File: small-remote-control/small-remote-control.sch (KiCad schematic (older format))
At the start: 9 parts, among them J1 AudioJack4, SW1 A, SW2 B, SW3 C, SW4 D

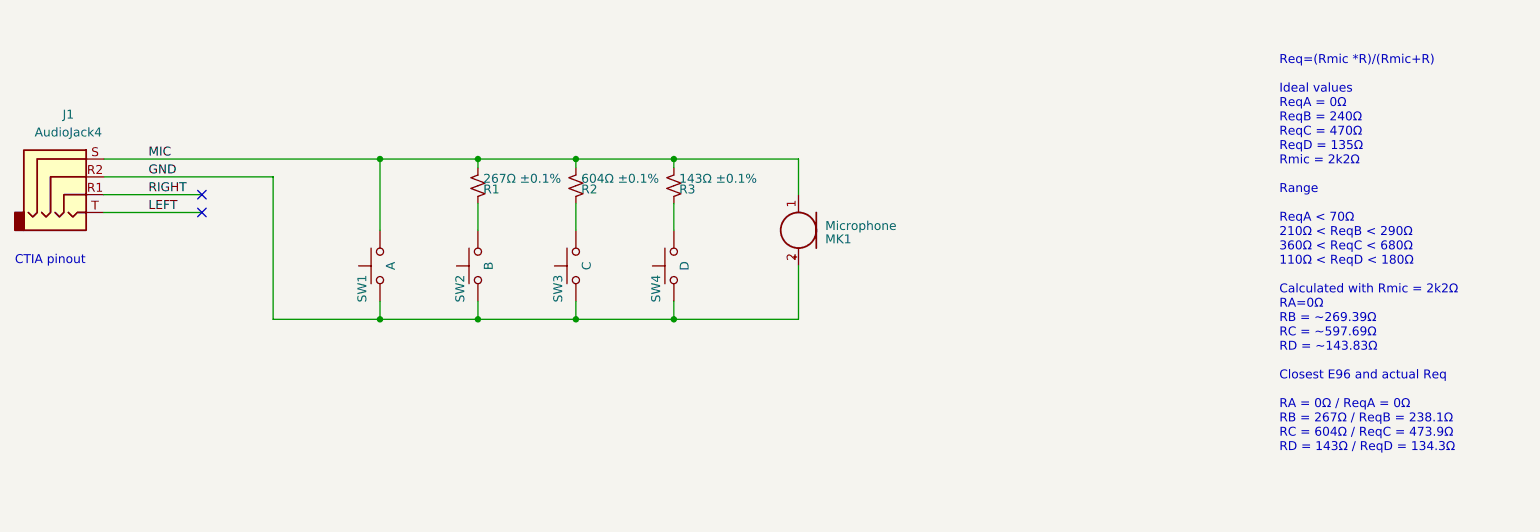
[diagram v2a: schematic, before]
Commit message: removed mic and switch D, added 2.2kΩ resistor
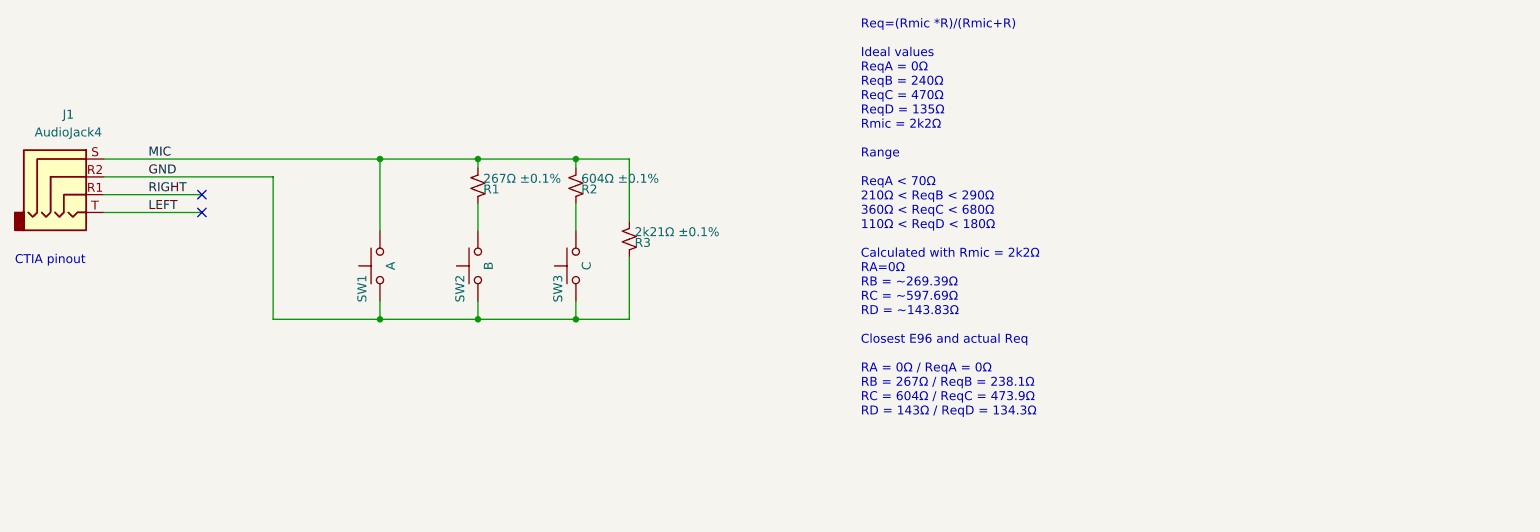
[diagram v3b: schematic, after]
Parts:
- removed MK1: Microphone, SW-CUI-INC:CMC-4015-40P, symbol Device:Microphone
- removed SW4: D, SW-Omron:B3W-6x6mm-NG, symbol Switch:SW_Push
- R3: value 143Ω ±0.1% -> 2k21Ω ±0.1%; Description RES 143 OHM 0.1% 1/10W 0402 -> RES 2.21K OHM 0.1% 1/10W 0402; MPN RP73PF1E143RBTD -> RP73PF1E2K21BTD
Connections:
- net GND: now also R3.1
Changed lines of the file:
@@
-$EndComp
-$Comp
-L Switch:SW_Push SW4
-U 1 1 5F24FFE6
-P 4600 3350
-F 0 "SW4" H 4650 3450 50  0000 L CNN
-F 1 "D" H 4600 3290 50  0000 C CNN
-F 2 "SW-Omron:B3W-6x6mm-NG" H 4600 3550 50  0001 C CNN
-F 3 "https://omronfs.omron.com/en_US/ecb/products/pdf/en-b3w.pdf" H 4600 3550 50  0001 C CNN
-F 4 "B3W-1002" H 4600 3350 50  0001 C CNN "MPN"
-F 5 "SWITCH TACTILE SPST-NO 0.05A 24V" H 4600 3350 50  0001 C CNN "Description"
-F 6 "Omron Electronics Inc-EMC Div" H 4600 3350 50  0001 C CNN "Manufacturer"
-F 7 "Digikey" H 4600 3350 50  0001 C CNN "Source"
-	1    4600 3350
-	0    -1   1    0
-$EndComp
-$Comp
-L Device:Microphone MK1
-U 1 1 5F25357C
-P 5300 3150
-F 0 "MK1" H 5150 3200 50  0000 R CNN
-F 1 "Microphone" H 5150 3125 50  0000 R CNN
-F 2 "SW-CUI-INC:CMC-4015-40P" V 5300 3250 50  0001 C CNN
-F 3 "https://www.cuidevices.com/product/resource/cmc-4015-40p.pdf" V 5300 3250 50  0001 C CNN
-F 4 "CUI Devices" H 5300 3150 50  0001 C CNN "Manufacturer"
-F 5 "Digikey" H 5300 3150 50  0001 C CNN "Source"
-F 6 "CMC-4015-40P" H 5300 3150 50  0001 C CNN "MPN"
-F 7 "(-40dB ±3dB @ 94dB SPL)" H 5300 3150 50  0001 C CNN "Characteristics"
-F 8 "100Hz ~ 20kHz Analog Microphone Electret Condenser 2V ~ 10V Omnidirectional (-40dB ±3dB @ 94dB SPL) PC Pins" H 5300 3150 50  0001 C CNN "Description"
-	1    5300 3150
-	-1   0    0    1
 $EndComp
 $Comp
@@
 	1    0    0    1
 $EndComp
-$Comp
-L Device:R_Small_US R3
-U 1 1 5F254B04
-P 4600 2900
-F 0 "R3" H 4630 2920 50  0000 L CNN
-F 1 "143Ω ±0.1%" H 4630 2860 50  0000 L CNN
-F 2 "Resistor_SMD:R_0402_1005Metric" H 4600 2900 50  0001 C CNN
-F 3 "~" H 4600 2900 50  0001 C CNN
-F 4 "TE Connectivity" H 4600 2900 50  0001 C CNN "Manufacturer"
-F 5 "0402/1005M" H 4600 2900 50  0001 C CNN "Package ID"
-F 6 "Digikey" H 4600 2900 50  0001 C CNN "Source"
-F 7 "RP73PF1E143RBTD" H 4600 2900 50  0001 C CNN "MPN"
-F 8 "RES 143 OHM 0.1% 1/10W 0402" H 4600 2900 50  0001 C CNN "Description"
-F 9 "0.1% 1/10W" H 4600 2900 50  0001 C CNN "Characteristics"
-	1    4600 2900
-	1    0    0    1
-$EndComp
 Text Label 1650 3050 0    50   ~ 0
 LEFT
@@
 Text Notes 900  3350 0    50   ~ 0
 CTIA pinout
-Text Notes 8000 4400 0    50   ~ 0
+Text Notes 5650 4200 0    50   ~ 0
 Req=(Rmic *R)/(Rmic+R)\n\nIdeal values\nReqA = 0Ω\nReqB = 240Ω\nReqC = 470Ω\nReqD = 135Ω\nRmic = 2k2Ω\n\nRange\n\nReqA < 70Ω\n210Ω < ReqB < 290Ω\n360Ω < ReqC < 680Ω\n110Ω < ReqD < 180Ω\n\nCalculated with Rmic = 2k2Ω\nRA=0Ω\nRB = ~~269.39Ω\nRC = ~~597.69Ω\nRD = ~~143.83Ω\n\nClosest E96 and actual Req\n\nRA = 0Ω / ReqA = 0Ω\nRB = 267Ω / ReqB = 238.1Ω\nRC = 604Ω / ReqC = 473.9Ω\nRD = 143Ω / ReqD = 134.3Ω
-Wire Wire Line
-	4600 2750 4600 2800
 Wire Wire Line
 	1400 2750 2950 2750
@@
 	4050 2800 4050 2750
 Connection ~ 4050 2750
-Wire Wire Line
-	4050 2750 4600 2750
 Wire Wire Line
 	3500 2800 3500 2750
@@
 	2950 2750 3500 2750
 Wire Wire Line
-	5300 2950 5300 2750
-Wire Wire Line
-	5300 2750 4600 2750
-Connection ~ 4600 2750
-Wire Wire Line
 	2350 2850 2350 3650
 Wire Wire Line
 	2350 3650 2950 3650
-Wire Wire Line
-	5300 3650 5300 3350
 Wire Wire Line
 	1400 2850 2350 2850
@@
 	4050 3550 4050 3650
 Connection ~ 4050 3650
-Wire Wire Line
-	4050 3650 4600 3650
-Wire Wire Line
-	4600 3550 4600 3650
-Connection ~ 4600 3650
-Wire Wire Line
-	4600 3650 5300 3650
-Wire Wire Line
-	4600 3000 4600 3150
 Wire Wire Line
 	4050 3150 4050 3000
@@
 Wire Wire Line
 	1400 2950 1950 2950
+$Comp
+L Device:R_Small_US R3
+U 1 1 5F27B8E6
+P 4350 3200
+F 0 "R3" H 4380 3220 50  0000 L CNN
+F 1 "2k21Ω ±0.1%" H 4380 3160 50  0000 L CNN
+F 2 "Resistor_SMD:R_0402_1005Metric" H 4350 3200 50  0001 C CNN
+F 3 "~" H 4350 3200 50  0001 C CNN
+F 4 "TE Connectivity" H 4350 3200 50  0001 C CNN "Manufacturer"
+F 5 "0402/1005M" H 4350 3200 50  0001 C CNN "Package ID"
+F 6 "Digikey" H 4350 3200 50  0001 C CNN "Source"
+F 7 "RP73PF1E2K21BTD" H 4350 3200 50  0001 C CNN "MPN"
+F 8 "RES 2.21K OHM 0.1% 1/10W 0402" H 4350 3200 50  0001 C CNN "Description"
+F 9 "0.1% 1/10W" H 4350 3200 50  0001 C CNN "Characteristics"
+	1    4350 3200
+	1    0    0    1
+$EndComp
+Wire Wire Line
+	4350 3300 4350 3650
+Wire Wire Line
+	4350 2750 4350 3100
+Wire Wire Line
+	4050 2750 4350 2750
+Wire Wire Line
+	4050 3650 4350 3650
 $EndSCHEMATC

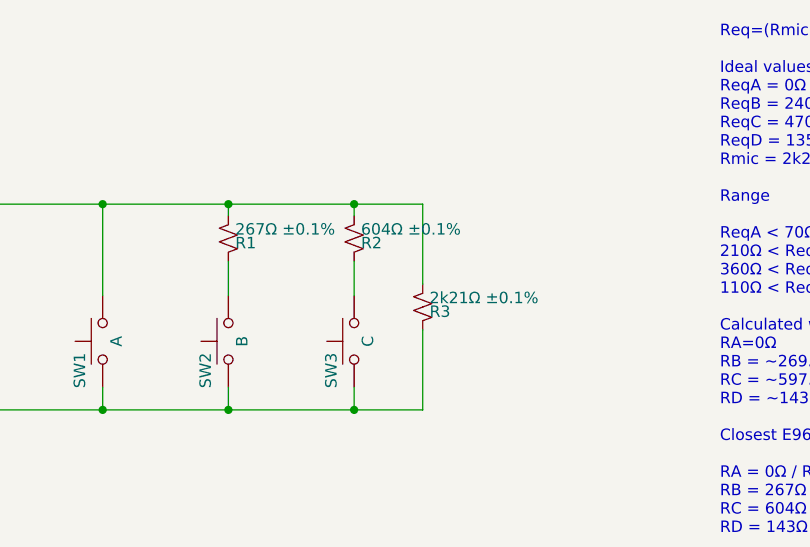
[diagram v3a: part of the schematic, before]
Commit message: switched to 0603 resistors
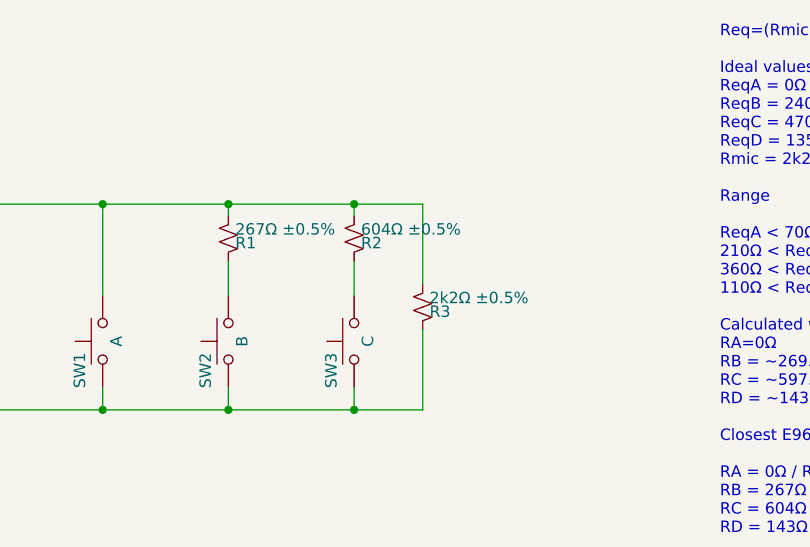
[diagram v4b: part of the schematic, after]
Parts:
- R1: value 267Ω ±0.1% -> 267Ω ±0.5%; footprint Resistor_SMD:R_0402_1005Metric -> Resistor_SMD:R_0603_1608Metric_Pad1.05x0.95mm_HandSolder; Characteristics 0.1% 1/10W -> 0.5% 1/16W; Description RES 267 OHM 0.1% 1/10W 0402 -> RES SMD 267 OHM 0.5% 1/16W 0603; MPN RP73PF1E267RBTD -> RR0816P-2670-D-42A; Manufacturer TE Connectivity -> Susumu; Package ID 0402/1005M -> 0603/1608M
- R2: value 604Ω ±0.1% -> 604Ω ±0.5%; footprint Resistor_SMD:R_0402_1005Metric -> Resistor_SMD:R_0603_1608Metric_Pad1.05x0.95mm_HandSolder; Characteristics 0.1% 1/10W -> 0.5% 1/16W; Description RES 604 OHM 0.1% 1/10W 0402 -> RES SMD 604 OHM 0.5% 1/16W 0603; MPN RP73PF1E604RBTD -> RR0816P-6040-D-76A; Manufacturer TE Connectivity -> Susumu; Package ID 0402/1005M -> 0603/1608M
- R3: value 2k21Ω ±0.1% -> 2k2Ω ±0.5%; footprint Resistor_SMD:R_0402_1005Metric -> Resistor_SMD:R_0603_1608Metric_Pad1.05x0.95mm_HandSolder; Characteristics 0.1% 1/10W -> 0.5% 1/16W; Description RES 2.21K OHM 0.1% 1/10W 0402 -> RES SMD 2.2K OHM 0.5% 1/16W 0603; MPN RP73PF1E2K21BTD -> RR0816P-222-D; Manufacturer TE Connectivity -> Susumu; Package ID 0402/1005M -> 0603/1608M
- SW1, SW2, SW3: Characteristics (none) -> SPST MOM NO
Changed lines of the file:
@@
 F 6 "Omron Electronics Inc-EMC Div" H 2950 3350 50  0001 C CNN "Manufacturer"
 F 7 "Digikey" H 2950 3350 50  0001 C CNN "Source"
+F 8 "SPST MOM NO" H 2950 3350 50  0001 C CNN "Characteristics"
 	1    2950 3350
 	0    -1   1    0
@@
 F 6 "Omron Electronics Inc-EMC Div" H 3500 3350 50  0001 C CNN "Manufacturer"
 F 7 "Digikey" H 3500 3350 50  0001 C CNN "Source"
+F 8 "SPST MOM NO" H 3500 3350 50  0001 C CNN "Characteristics"
 	1    3500 3350
 	0    -1   1    0
@@
 F 6 "Omron Electronics Inc-EMC Div" H 4050 3350 50  0001 C CNN "Manufacturer"
 F 7 "Digikey" H 4050 3350 50  0001 C CNN "Source"
+F 8 "SPST MOM NO" H 4050 3350 50  0001 C CNN "Characteristics"
 	1    4050 3350
 	0    -1   1    0
@@
 P 3500 2900
 F 0 "R1" H 3530 2920 50  0000 L CNN
-F 1 "267Ω ±0.1%" H 3530 2860 50  0000 L CNN
-F 2 "Resistor_SMD:R_0402_1005Metric" H 3500 2900 50  0001 C CNN
-F 3 "~" H 3500 2900 50  0001 C CNN
-F 4 "RES 267 OHM 0.1% 1/10W 0402" H 3500 2900 50  0001 C CNN "Description"
-F 5 "RP73PF1E267RBTD" H 3500 2900 50  0001 C CNN "MPN"
-F 6 "TE Connectivity" H 3500 2900 50  0001 C CNN "Manufacturer"
-F 7 "0402/1005M" H 3500 2900 50  0001 C CNN "Package ID"
+F 1 "267Ω ±0.5%" H 3530 2860 50  0000 L CNN
+F 2 "Resistor_SMD:R_0603_1608Metric_Pad1.05x0.95mm_HandSolder" H 3500 2900 50  0001 C CNN
+F 3 "https://www.susumu.co.jp/common/pdf/n_catalog_partition05_en.pdf" H 3500 2900 50  0001 C CNN
+F 4 "RES SMD 267 OHM 0.5% 1/16W 0603" H 3500 2900 50  0001 C CNN "Description"
+F 5 "RR0816P-2670-D-42A" H 3500 2900 50  0001 C CNN "MPN"
+F 6 "Susumu" H 3500 2900 50  0001 C CNN "Manufacturer"
+F 7 "0603/1608M" H 3500 2900 50  0001 C CNN "Package ID"
 F 8 "Digikey" H 3500 2900 50  0001 C CNN "Source"
-F 9 "0.1% 1/10W" H 3500 2900 50  0001 C CNN "Characteristics"
+F 9 "0.5% 1/16W" H 3500 2900 50  0001 C CNN "Characteristics"
 	1    3500 2900
 	1    0    0    1
@@
 P 4050 2900
 F 0 "R2" H 4080 2920 50  0000 L CNN
-F 1 "604Ω ±0.1%" H 4080 2860 50  0000 L CNN
-F 2 "Resistor_SMD:R_0402_1005Metric" H 4050 2900 50  0001 C CNN
-F 3 "~" H 4050 2900 50  0001 C CNN
-F 4 "RES 604 OHM 0.1% 1/10W 0402" H 4050 2900 50  0001 C CNN "Description"
-F 5 "RP73PF1E604RBTD" H 4050 2900 50  0001 C CNN "MPN"
-F 6 "TE Connectivity" H 4050 2900 50  0001 C CNN "Manufacturer"
-F 7 "0402/1005M" H 4050 2900 50  0001 C CNN "Package ID"
+F 1 "604Ω ±0.5%" H 4080 2860 50  0000 L CNN
+F 2 "Resistor_SMD:R_0603_1608Metric_Pad1.05x0.95mm_HandSolder" H 4050 2900 50  0001 C CNN
+F 3 "https://www.susumu.co.jp/common/pdf/n_catalog_partition05_en.pdf" H 4050 2900 50  0001 C CNN
+F 4 "RES SMD 604 OHM 0.5% 1/16W 0603" H 4050 2900 50  0001 C CNN "Description"
+F 5 "RR0816P-6040-D-76A" H 4050 2900 50  0001 C CNN "MPN"
+F 6 "Susumu" H 4050 2900 50  0001 C CNN "Manufacturer"
+F 7 "0603/1608M" H 4050 2900 50  0001 C CNN "Package ID"
 F 8 "Digikey" H 4050 2900 50  0001 C CNN "Source"
-F 9 "0.1% 1/10W" H 4050 2900 50  0001 C CNN "Characteristics"
+F 9 "0.5% 1/16W" H 4050 2900 50  0001 C CNN "Characteristics"
 	1    4050 2900
 	1    0    0    1
@@
 P 4350 3200
 F 0 "R3" H 4380 3220 50  0000 L CNN
-F 1 "2k21Ω ±0.1%" H 4380 3160 50  0000 L CNN
-F 2 "Resistor_SMD:R_0402_1005Metric" H 4350 3200 50  0001 C CNN
-F 3 "~" H 4350 3200 50  0001 C CNN
-F 4 "TE Connectivity" H 4350 3200 50  0001 C CNN "Manufacturer"
-F 5 "0402/1005M" H 4350 3200 50  0001 C CNN "Package ID"
+F 1 "2k2Ω ±0.5%" H 4380 3160 50  0000 L CNN
+F 2 "Resistor_SMD:R_0603_1608Metric_Pad1.05x0.95mm_HandSolder" H 4350 3200 50  0001 C CNN
+F 3 "https://www.susumu.co.jp/common/pdf/n_catalog_partition05_en.pdf" H 4350 3200 50  0001 C CNN
+F 4 "Susumu" H 4350 3200 50  0001 C CNN "Manufacturer"
+F 5 "0603/1608M" H 4350 3200 50  0001 C CNN "Package ID"
 F 6 "Digikey" H 4350 3200 50  0001 C CNN "Source"
-F 7 "RP73PF1E2K21BTD" H 4350 3200 50  0001 C CNN "MPN"
-F 8 "RES 2.21K OHM 0.1% 1/10W 0402" H 4350 3200 50  0001 C CNN "Description"
-F 9 "0.1% 1/10W" H 4350 3200 50  0001 C CNN "Characteristics"
+F 7 "RR0816P-222-D" H 4350 3200 50  0001 C CNN "MPN"
+F 8 "RES SMD 2.2K OHM 0.5% 1/16W 0603" H 4350 3200 50  0001 C CNN "Description"
+F 9 "0.5% 1/16W" H 4350 3200 50  0001 C CNN "Characteristics"
 	1    4350 3200
 	1    0    0    1
